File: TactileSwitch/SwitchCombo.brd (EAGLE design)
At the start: 13 x 11.6 mm, 4 parts, among them J1 CONN_3, J2 CONN_3

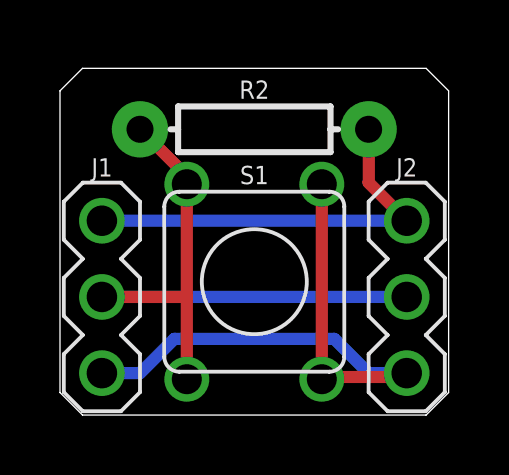
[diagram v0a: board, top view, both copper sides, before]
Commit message: Updated tactile switch combo resistor
Changed the resistor layout on the combo switch breakout to be more relaxed and work more easily with standard 1/4 W resistors
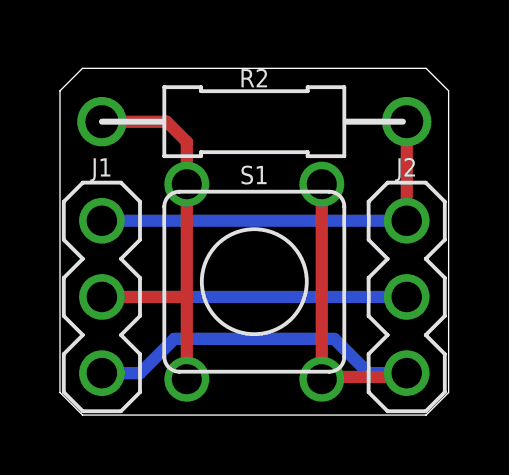
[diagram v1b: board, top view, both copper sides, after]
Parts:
- R2: device SparkFun-Resistors:AXIAL-0.3 -> bschulz_passives:R_TH_0.4"
- moved R2 0.25 mm to (6.48, 9.78)
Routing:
- net P2: track 22.0 -> 24.0 mm
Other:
- board text added: "v0.1"
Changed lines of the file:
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@@
 <?xml version="1.0" encoding="utf-8"?>
 <!DOCTYPE eagle SYSTEM "eagle.dtd">
-<eagle version="9.4.2">
+<eagle version="9.6.2">
 <drawing>
 <settings>
@@
 <layer number="20" name="Dimension" color="24" fill="1" visible="yes" active="yes"/>
 <layer number="21" name="tPlace" color="7" fill="1" visible="yes" active="yes"/>
-<layer number="22" name="bPlace" color="7" fill="1" visible="no" active="yes"/>
+<layer number="22" name="bPlace" color="7" fill="1" visible="yes" active="yes"/>
 <layer number="23" name="tOrigins" color="15" fill="1" visible="yes" active="yes"/>
-<layer number="24" name="bOrigins" color="15" fill="1" visible="no" active="yes"/>
+<layer number="24" name="bOrigins" color="15" fill="1" visible="yes" active="yes"/>
 <layer number="25" name="tNames" color="7" fill="1" visible="yes" active="yes"/>
-<layer number="26" name="bNames" color="7" fill="1" visible="no" active="yes"/>
+<layer number="26" name="bNames" color="7" fill="1" visible="yes" active="yes"/>
 <layer number="27" name="tValues" color="7" fill="1" visible="no" active="yes"/>
 <layer number="28" name="bValues" color="7" fill="1" visible="no" active="yes"/>
@@
 <layer number="38" name="bTest" color="7" fill="1" visible="no" active="yes"/>
 <layer number="39" name="tKeepout" color="4" fill="11" visible="yes" active="yes"/>
-<layer number="40" name="bKeepout" color="1" fill="11" visible="no" active="yes"/>
+<layer number="40" name="bKeepout" color="1" fill="11" visible="yes" active="yes"/>
 <layer number="41" name="tRestrict" color="4" fill="10" visible="yes" active="yes"/>
-<layer number="42" name="bRestrict" color="1" fill="10" visible="no" active="yes"/>
+<layer number="42" name="bRestrict" color="1" fill="10" visible="yes" active="yes"/>
 <layer number="43" name="vRestrict" color="2" fill="10" visible="no" active="yes"/>
 <layer number="44" name="Drills" color="7" fill="1" visible="no" active="yes"/>
-<layer number="45" name="Holes" color="7" fill="1" visible="yes" active="yes"/>
+<layer number="45" name="Holes" color="7" fill="1" visible="no" active="yes"/>
 <layer number="46" name="Milling" color="3" fill="1" visible="no" active="yes"/>
 <layer number="47" name="Measures" color="7" fill="1" visible="no" active="yes"/>
@@
 <layer number="50" name="dxf" color="7" fill="1" visible="no" active="no"/>
 <layer number="51" name="tDocu" color="7" fill="1" visible="yes" active="yes"/>
-<layer number="52" name="bDocu" color="7" fill="1" visible="no" active="yes"/>
+<layer number="52" name="bDocu" color="7" fill="1" visible="yes" active="yes"/>
 <layer number="53" name="tGND_GNDA" color="7" fill="1" visible="no" active="no"/>
 <layer number="54" name="bGND_GNDA" color="7" fill="1" visible="no" active="no"/>
@@
 <layer number="115" name="ReferenceISLANDS" color="7" fill="1" visible="no" active="yes"/>
 <layer number="116" name="Patch_BOT" color="7" fill="1" visible="no" active="yes"/>
+<layer number="117" name="PM_Ref" color="7" fill="1" visible="no" active="no"/>
 <layer number="118" name="Rect_Pads" color="7" fill="1" visible="no" active="yes"/>
+<layer number="119" name="PF_Ref" color="7" fill="1" visible="no" active="no"/>
+<layer number="120" name="WFL_Ref" color="7" fill="1" visible="no" active="no"/>
 <layer number="121" name="_tsilk" color="7" fill="1" visible="no" active="yes"/>
 <layer number="122" name="_bsilk" color="7" fill="1" visible="no" active="yes"/>
@@
 <text x="9.906" y="3.937" size="0.8128" layer="51" font="vector" ratio="15" align="center">2</text>
 <text x="9.906" y="1.27" size="0.8128" layer="51" font="vector" ratio="15" align="center">1</text>
+<text x="2.794" y="10.795" size="0.6096" layer="52" font="vector" ratio="15" rot="MR0">v0.1</text>
 </plain>
 <attributes>
@@
 <attribute name="NAME" x="11.557" y="8.255" size="0.6096" layer="25" font="vector" ratio="20" align="center"/>
 </element>
-<element name="R2" library="SparkFun-Resistors" library_urn="urn:adsk.eagle:library:532" package="AXIAL-0.3" package3d_urn="urn:adsk.eagle:package:39658/1" value="10k" x="6.477" y="9.525" smashed="yes">
-<attribute name="NAME" x="6.477" y="10.541" size="0.6096" layer="25" font="vector" ratio="20" align="bottom-center"/>
-<attribute name="PROD_ID" value="RES-12183" x="6.477" y="9.525" size="0.8128" layer="27" font="vector" ratio="15" display="off"/>
-<attribute name="VALUE" x="6.477" y="8.509" size="0.6096" layer="27" font="vector" ratio="20" align="top-center"/>
+<element name="R2" library="bschulz_passives" package="R_TH_0.4&quot;" value="10k" x="6.477" y="9.779" smashed="yes">
+<attribute name="NAME" x="6.477" y="10.922" size="0.6096" layer="25" font="vector" ratio="15" align="bottom-center"/>
 </element>
 </elements>
@@
 <contactref element="S1" pad="2"/>
 <contactref element="R2" pad="P$1"/>
-<wire x1="2.667" y1="9.525" x2="4.227" y2="7.965" width="0.4064" layer="1"/>
-<wire x1="4.227" y1="7.965" x2="4.227" y2="7.695" width="0.4064" layer="1"/>
 <wire x1="4.227" y1="1.195" x2="4.227" y2="3.937" width="0.4064" layer="1"/>
 <wire x1="4.227" y1="3.937" x2="4.227" y2="7.695" width="0.4064" layer="1"/>
 <wire x1="1.397" y1="3.937" x2="4.227" y2="3.937" width="0.4064" layer="1"/>
 <wire x1="1.397" y1="3.937" x2="11.557" y2="3.937" width="0.4064" layer="16"/>
+<wire x1="1.397" y1="9.779" x2="3.556" y2="9.779" width="0.4064" layer="1"/>
+<wire x1="4.227" y1="9.108" x2="4.227" y2="7.695" width="0.4064" layer="1"/>
+<wire x1="3.556" y1="9.779" x2="4.227" y2="9.108" width="0.4064" layer="1"/>
 </signal>
 <signal name="P3">
@@
 <contactref element="J2" pad="1"/>
 <contactref element="R2" pad="P$2"/>
-<wire x1="11.557" y1="6.477" x2="10.287" y2="7.747" width="0.4064" layer="1"/>
-<wire x1="10.287" y1="7.747" x2="10.287" y2="9.525" width="0.4064" layer="1"/>
 <wire x1="1.397" y1="6.477" x2="11.557" y2="6.477" width="0.4064" layer="16"/>
+<wire x1="11.557" y1="6.477" x2="11.557" y2="9.779" width="0.4064" layer="1"/>
 </signal>
 </signals>
@@
 which will not be processed correctly with this version.
 </note>
-<note version="8.2" severity="warning">
-Since Version 8.2, EAGLE supports online libraries. The ids
-of those online libraries will not be understood (or retained)
-with this version.
-</note>
-<note version="8.3" severity="warning">
-Since Version 8.3, EAGLE supports URNs for individual library
-assets (packages, symbols, and devices). The URNs of those assets
-will not be understood (or retained) with this version.
-</note>
-<note version="8.3" severity="warning">
-Since Version 8.3, EAGLE supports the association of 3D packages
-with devices in libraries, schematics, and board files. Those 3D
-packages will not be understood (or retained) with this version.
-</note>
 </compatibility>
